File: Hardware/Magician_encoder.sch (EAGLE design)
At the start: 29 parts, among them Q1 MMBT2222A, Q2 MMBT2222A, U1 QRE1113, U2 QRE1113

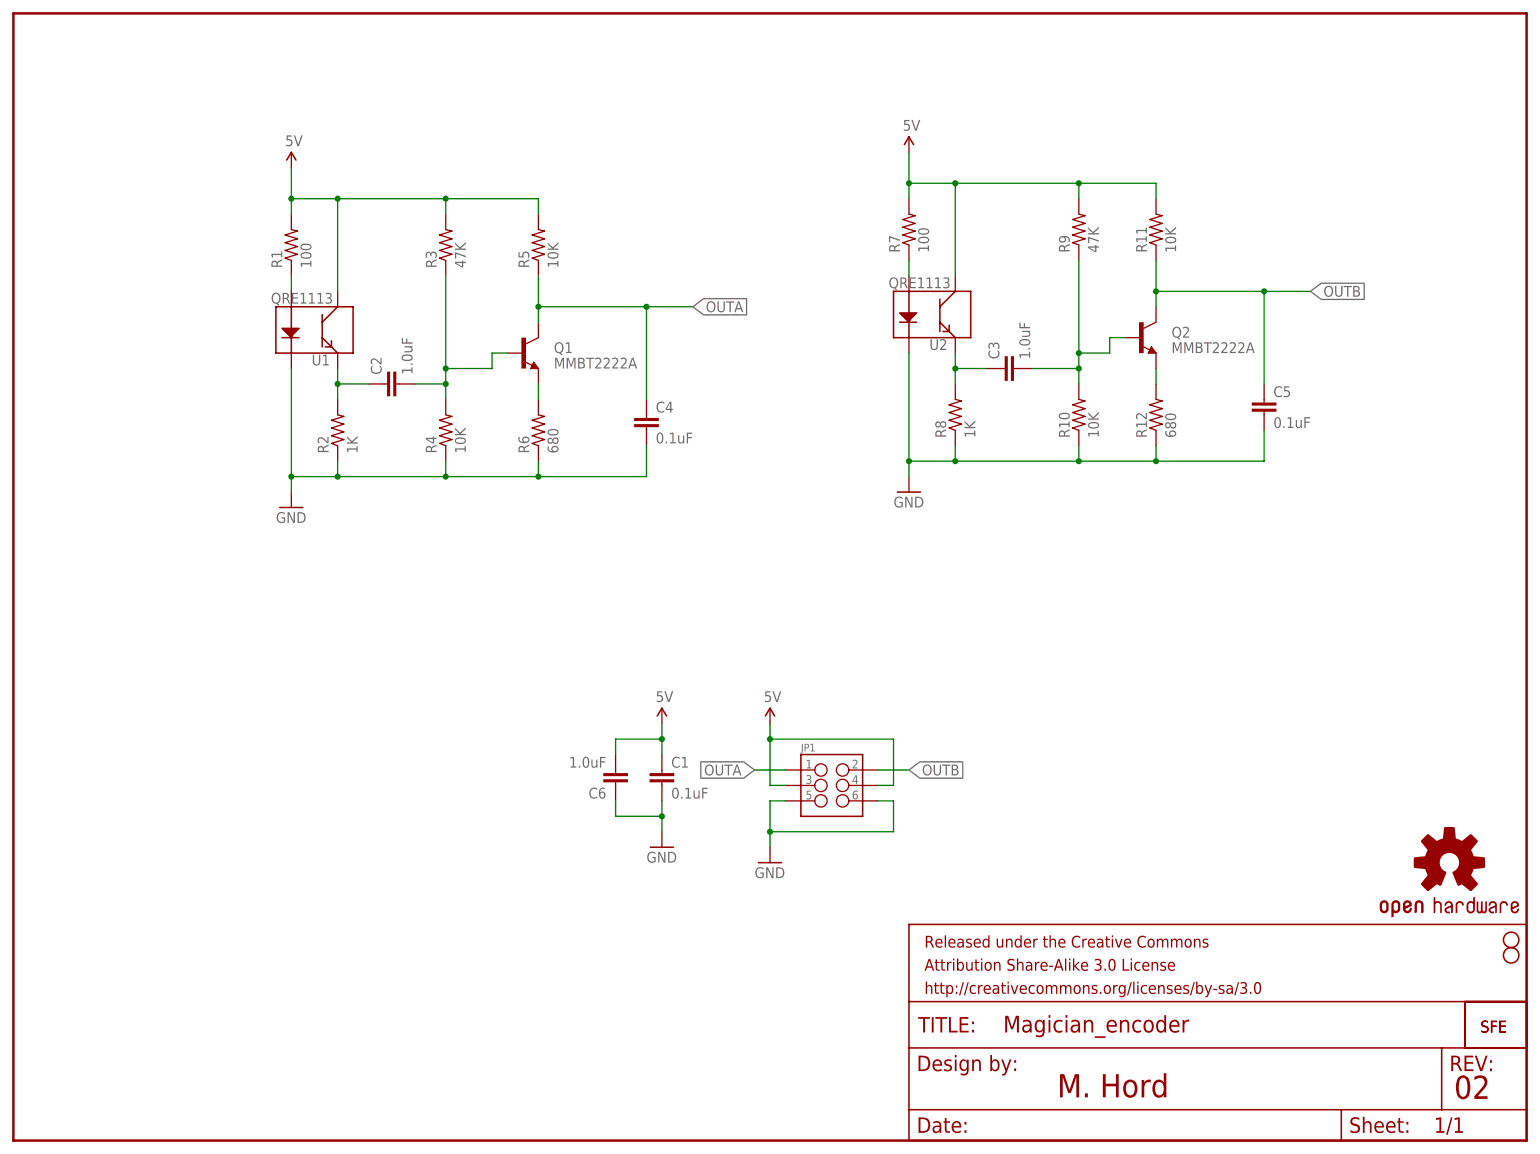
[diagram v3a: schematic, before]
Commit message: Update values and circuit for better performance
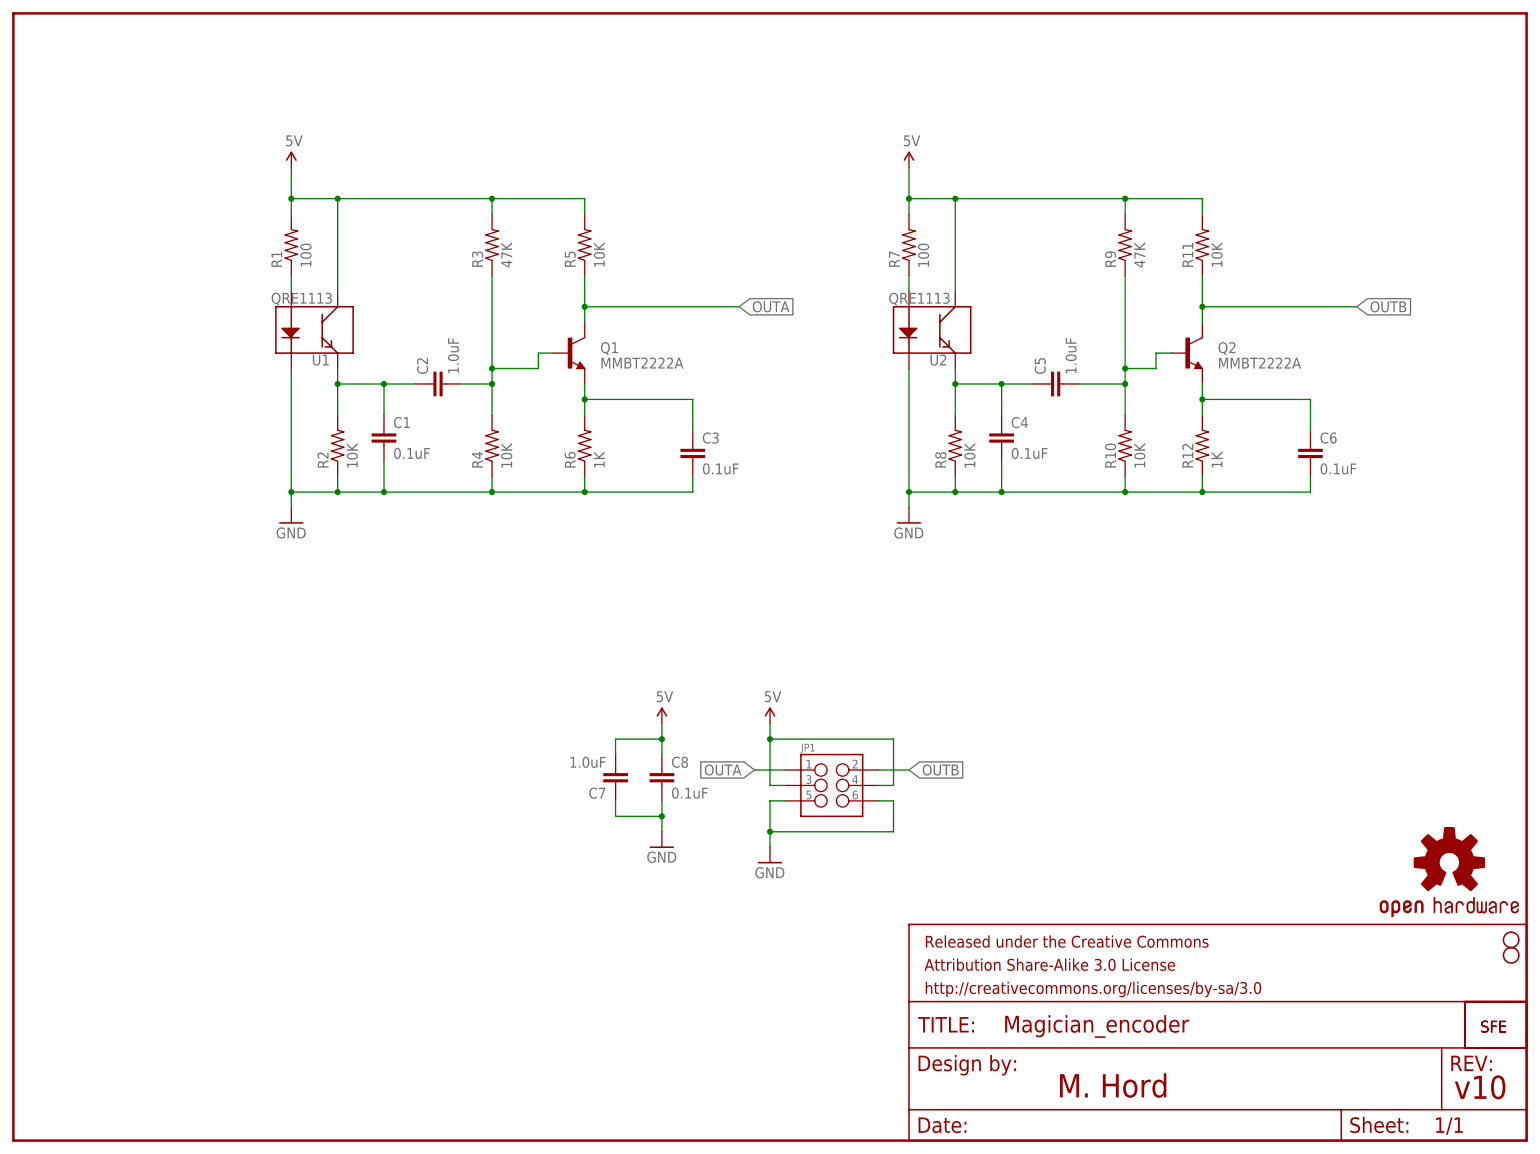
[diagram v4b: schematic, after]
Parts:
- added C7: 1.0uF, SparkFun-Capacitors:1.0UF-16V-10%(0603)
- added C8: 0.1uF, SparkFun-Capacitors:0.1UF-25V(+80/-20%)(0603)
- C3, C6: value 1.0uF -> 0.1uF; device SparkFun-Capacitors:1.0UF-16V-10%(0603) -> SparkFun-Capacitors:0.1UF-25V(+80/-20%)(0603)
- C5: value 0.1uF -> 1.0uF; device SparkFun-Capacitors:0.1UF-25V(+80/-20%)(0603) -> SparkFun-Capacitors:1.0UF-16V-10%(0603)
- R12, R6: value 680 -> 1K; device SparkFun-Resistors:680OHM1/10W5%(0603) -> SparkFun-Resistors:1KOHM1/10W1%(0603)
- R2, R8: value 1K -> 10K; device SparkFun-Resistors:1KOHM1/10W1%(0603) -> SparkFun-Resistors:10KOHM1/10W1%(0603)0603
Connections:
- net 5V: now also C7.2, C8.1; no longer C1.1, C6.2
- net GND: now also C3.2, C6.2, C7.1, C8.2; no longer C5.2, C6.1
- net N$1: now also C1.1
- net N$3: now also C3.1
- net N$7: now also C6.1
- net N$8: now also C4.1, C5.1; no longer C3.1
- net N$9: now also C5.2; no longer C3.2
- net OUTA: no longer C4.1
- net OUTB: no longer C5.1
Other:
- note added: "v10"
- note removed: "02"
- moved on the sheet: C1, C2, C3, C4, C5, C6, Q1, Q2, R10, R11, R12, R2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

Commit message: Update schematic with prod. values
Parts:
- R10, R4: value 10K -> 6.8K; PROD_ID (none) -> RES-08597
- R11, R5: value 10K -> 4.7K; PROD_ID (none) -> RES-07857
- R12, R6: value 1K -> 100; PROD_ID (none) -> RES-07863
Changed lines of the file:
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@@
 <part name="C2" library="SparkFun-Capacitors" deviceset="1.0UF-16V-10%(0603)" device="" value="1.0uF"/>
 <part name="R3" library="SparkFun-Resistors" deviceset="47KOHM1/10W1%(0603)" device="" value="47K"/>
-<part name="R4" library="SparkFun-Resistors" deviceset="10KOHM1/10W1%(0603)" device="0603" value="10K"/>
-<part name="R5" library="SparkFun-Resistors" deviceset="10KOHM1/10W1%(0603)" device="0603" value="10K"/>
-<part name="R12" library="SparkFun-Resistors" deviceset="1KOHM1/10W1%(0603)" device="" value="1K"/>
+<part name="R4" library="SparkFun-Resistors" deviceset="10KOHM1/10W1%(0603)" device="0603" value="6.8K">
+<attribute name="PROD_ID" value="RES-08597"/>
+</part>
+<part name="R5" library="SparkFun-Resistors" deviceset="10KOHM1/10W1%(0603)" device="0603" value="4.7K">
+<attribute name="PROD_ID" value="RES-07857"/>
+</part>
+<part name="R12" library="SparkFun-Resistors" deviceset="1KOHM1/10W1%(0603)" device="" value="100">
+<attribute name="PROD_ID" value="RES-07863"/>
+</part>
 <part name="C5" library="SparkFun-Capacitors" deviceset="1.0UF-16V-10%(0603)" device="" value="1.0uF"/>
 <part name="R9" library="SparkFun-Resistors" deviceset="47KOHM1/10W1%(0603)" device="" value="47K"/>
-<part name="R10" library="SparkFun-Resistors" deviceset="10KOHM1/10W1%(0603)" device="0603" value="10K"/>
-<part name="R11" library="SparkFun-Resistors" deviceset="10KOHM1/10W1%(0603)" device="0603" value="10K"/>
+<part name="R10" library="SparkFun-Resistors" deviceset="10KOHM1/10W1%(0603)" device="0603" value="6.8K">
+<attribute name="PROD_ID" value="RES-08597"/>
+</part>
+<part name="R11" library="SparkFun-Resistors" deviceset="10KOHM1/10W1%(0603)" device="0603" value="4.7K">
+<attribute name="PROD_ID" value="RES-07857"/>
+</part>
 <part name="C3" library="SparkFun-Capacitors" deviceset="0.1UF-25V(+80/-20%)(0603)" device="" value="0.1uF"/>
 <part name="C6" library="SparkFun-Capacitors" deviceset="0.1UF-25V(+80/-20%)(0603)" device="" value="0.1uF"/>
@@
 <part name="Q2" library="SparkFun-DiscreteSemi" deviceset="TRANSISTOR_NPN" device="MMBT2222A" value="MMBT2222A"/>
 <part name="LOGO1" library="SparkFun-Aesthetics" deviceset="LOGO-SFE" device="SK"/>
-<part name="R6" library="SparkFun-Resistors" deviceset="1KOHM1/10W1%(0603)" device="" value="1K"/>
+<part name="R6" library="SparkFun-Resistors" deviceset="1KOHM1/10W1%(0603)" device="" value="100">
+<attribute name="PROD_ID" value="RES-07863"/>
+</part>
 <part name="R2" library="SparkFun-Resistors" deviceset="10KOHM1/10W1%(0603)" device="0603" value="10K"/>
 <part name="C1" library="SparkFun-Capacitors" deviceset="0.1UF-25V(+80/-20%)(0603)" device="" value="0.1uF"/>
